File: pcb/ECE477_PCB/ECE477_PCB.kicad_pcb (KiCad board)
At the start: 2 copper layers, 36.5 x 25.4 mm, 64 parts, among them J1 PWR, J2 USB_B_Micro, J3 Micro_SD_Card_Det, J4 DEBUG, J5 DSMX, M1 Brushed_DC, M2 Brushed_DC, M3 Brushed_DC, M4 Brushed_DC, Q1 IRLML6244TR, Q2 IRLML6244TR, Q3 IRLML6244TR, Q4 IRLML6244TR, SW1 SW_Push, U1 AMS1117-3.3, U3 FT230XQ, U4 STM32F446RETx, U5 MPU-6050, Y1 16MHz X322516MLB4SI

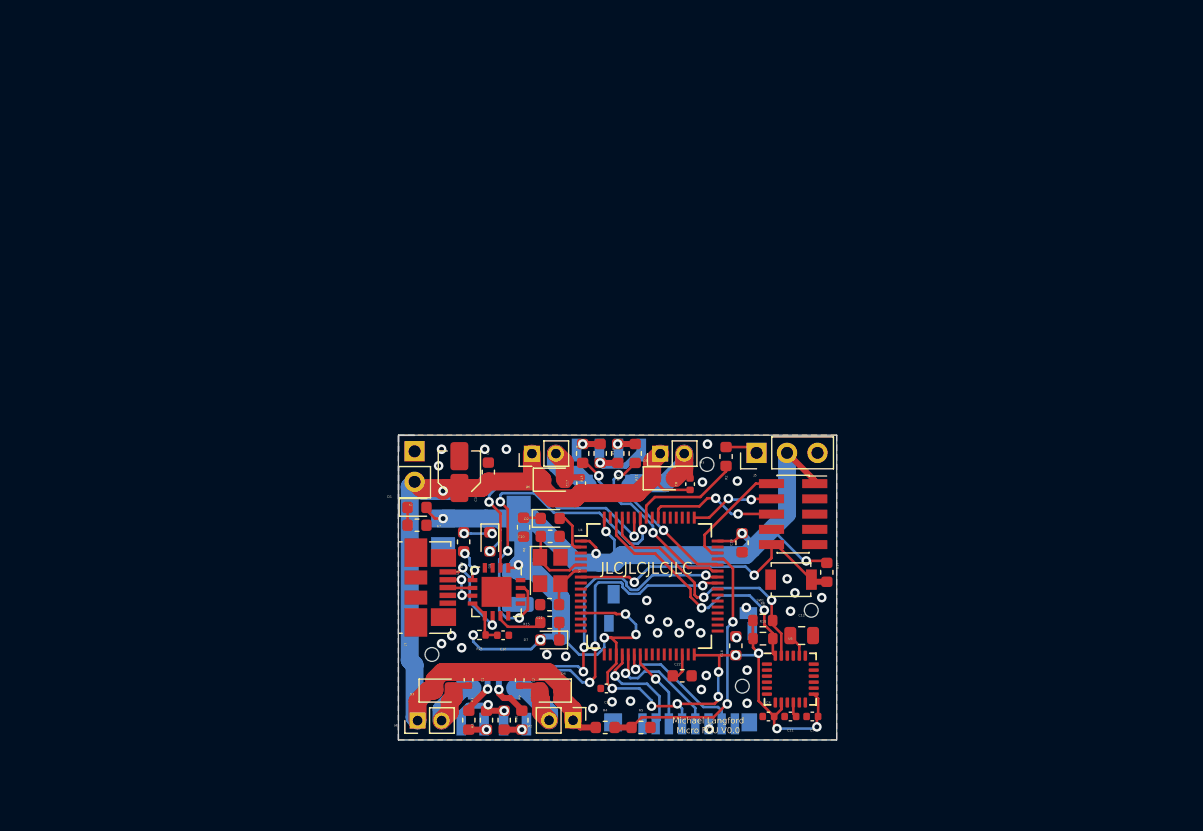
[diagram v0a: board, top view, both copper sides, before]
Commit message: updated PCB to Kicad 6
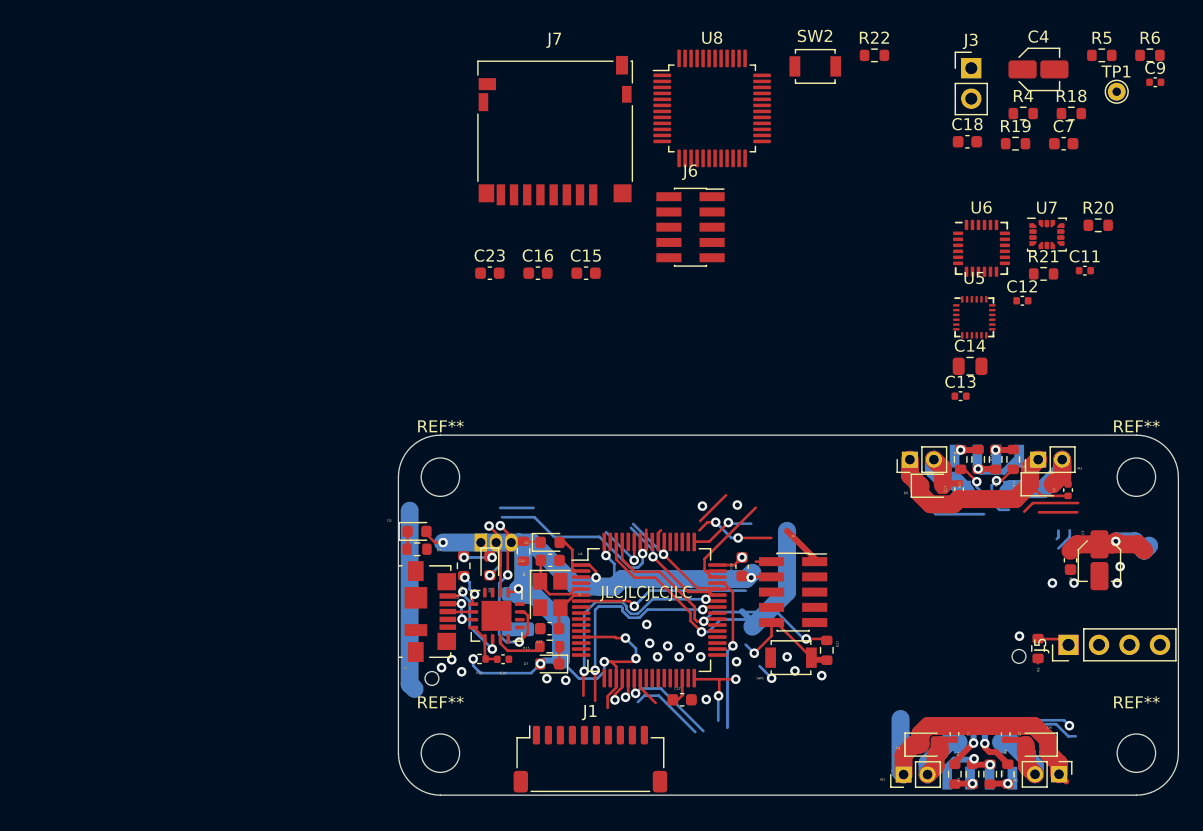
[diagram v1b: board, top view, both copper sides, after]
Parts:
- added C13: 0.1uF 2V, Capacitor_SMD:C_0402_1005Metric, F.Cu at (94.8, 24.7)
- added C14: 2.2nF, 50V, Capacitor_SMD:C_0805_2012Metric, F.Cu at (95.5, 22.2)
- added C15: 2.2uF, Capacitor_SMD:C_0603_1608Metric, F.Cu at (63.5, 14.5)
- added C16: 1uF, Capacitor_SMD:C_0603_1608Metric, F.Cu at (59.5, 14.5)
- added C23: 10nF, Capacitor_SMD:C_0603_1608Metric, F.Cu at (55.5, 14.5)
- added J6: DEBUG, Connector_PinSocket_1.27mm:PinSocket_2x05_P1.27mm_Vertical_SMD, F.Cu at (72.2, 10.6)
- added J7: Micro_SD_Card_Det, Connector_Card:microSD_HC_Hirose_DM3D-SF, F.Cu at (61.0, 2.59)
- added R19: 220, Resistor_SMD:R_0603_1608Metric, F.Cu at (99.3, 3.68)
- added R20: 4.7K, Resistor_SMD:R_0603_1608Metric, F.Cu at (106.2, 10.5)
- added R21: 4.7K, Resistor_SMD:R_0603_1608Metric, F.Cu at (101.7, 14.5)
- added R22: 1K, Resistor_SMD:R_0603_1608Metric, F.Cu at (87.6, -3.68)
- added REF**: MountingHole_3.2mm_M3, MountingHole:MountingHole_3.2mm_M3, F.Cu at (109.4, 31.5)
- added REF**: MountingHole_3.2mm_M3, MountingHole:MountingHole_3.2mm_M3, F.Cu at (109.4, 54.5)
- added REF**: MountingHole_3.2mm_M3, MountingHole:MountingHole_3.2mm_M3, F.Cu at (51.4, 54.5)
- added REF**: MountingHole_3.2mm_M3, MountingHole:MountingHole_3.2mm_M3, F.Cu at (51.4, 31.5)
- added SW2: RESET, Button_Switch_SMD:SW_SPST_B3U-1000P, F.Cu at (82.6, -2.76)
- added TP1: TX, TestPoint:TestPoint_THTPad_D1.5mm_Drill0.7mm, F.Cu at (107.8, -0.65)
- added U6: MPU-6050, Sensor_Motion:InvenSense_QFN-24_4x4mm_P0.5mm, F.Cu at (96.5, 12.4)
- added U7: LSM6DS3, Package_LGA:LGA-14_3x2.5mm_P0.5mm_LayoutBorder3x4y, F.Cu at (101.9, 11.2)
- added U8: STM32F103CBTx, Package_QFP:LQFP-48_7x7mm_P0.5mm, F.Cu at (74.0, 0.74)
- C11: value 0.1uF 2V -> 10nF, 4V
- C12: value 2.2nF, 50V -> 0.1uF 4V; footprint Capacitor_SMD:C_0805_2012Metric -> Capacitor_SMD:C_0402_1005Metric
- C4: value 10nF, 4V -> 100uF; footprint Capacitor_SMD:C_0402_1005Metric -> Capacitor_SMD:C_Elec_3x5.4
- C7: value 0.1uF 4V -> 1uF; footprint Capacitor_SMD:C_0402_1005Metric -> Capacitor_SMD:C_0603_1608Metric
- J1: value PWR -> ESC; footprint Connector_PinHeader_2.54mm:PinHeader_1x02_P2.54mm_Vertical -> Connector_JST:JST_SH_SM10B-SRSS-TB_1x10-1MP_P1.00mm_Horizontal
- J3: value Micro_SD_Card_Det -> AUX_PWR; footprint Connector_Card:microSD_HC_Hirose_DM3D-SF -> Connector_PinHeader_2.54mm:PinHeader_1x02_P2.54mm_Vertical; moved to F.Cu
- J5: value DSMX -> ELRS; footprint Connector_PinHeader_2.54mm:PinHeader_1x03_P2.54mm_Vertical -> Connector_PinHeader_2.54mm:PinHeader_1x04_P2.54mm_Vertical
- R18: value 4.7K -> 220
- R6: value 4.7K -> 0 DNP
- SW1: value SW_Push -> RESET
- U1: value AMS1117-3.3 -> LM78L05_TO92; footprint Package_TO_SOT_SMD:SOT-223-3_TabPin2 -> Package_TO_SOT_THT:TO-92_Inline
- U5: value MPU-6050 -> MPU-9250; footprint Sensor_Motion:InvenSense_QFN-24_4x4mm_P0.5mm -> Sensor_Motion:InvenSense_QFN-24_3x3mm_P0.4mm
- moved C9 68.1 mm to (111.0, -1.44), turned to 0 degrees
- moved R5 67.9 mm to (106.5, -3.68)
- moved R4 61.9 mm to (100.0, 1.17)
- moved C4 58.4 mm to (101.2, -2.51)
- moved R6 57.1 mm to (110.5, -3.68)
- moved J3 54.9 mm to (95.6, -2.61), turned to 0 degrees
- moved C3 53.8 mm to (106.3, 38.4), turned to -90 degrees
- moved C7 52.1 mm to (103.3, 3.68), turned to 0 degrees
- moved R18 50.7 mm to (104.0, 1.17)
- moved C6 49.1 mm to (103.9, 38.4), turned to -90 degrees
- moved C18 46.2 mm to (95.3, 3.52), turned to 0 degrees
- moved C11 44.5 mm to (105.1, 14.3), turned to 0 degrees
- moved M2 40.7 mm to (103.0, 56.2)
- moved R3 40.7 mm to (95.7, 56.2)
- moved C2 40.7 mm to (98.5, 52.9)
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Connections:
- C11 pad 1: Net-(C11-Pad1) -> GND
- C11 pad 2: GND -> +3V3
- C12 pad 1: Net-(C12-Pad1) -> +3V3
- C3 pad 1: +BATT -> +10V
- C4 pad 1: GND -> +5V
- C4 pad 2: +3V3 -> GND
- C6 pad 1: +BATT -> +10V
- C7 pad 1: +3V3 -> +5V
- J1 pad 2: +BATT -> GND
- J2 pad 4: (no net) -> unconnected-(J2-Pad4)
- J3 pad 1: (no net) -> GND
- J3 pad 2: SD_CARD_CS -> +BATT
- J4 pad 7: (no net) -> unconnected-(J4-Pad7)
- J4 pad 8: (no net) -> unconnected-(J4-Pad8)
- J5 pad 2: +3V3 -> Net-(J5-Pad2)
- J5 pad 3: GND -> +5V
- R18 pad 1: +3V3 -> Net-(R4-Pad2)
- R18 pad 2: I2C1_SDA -> unconnected-(R18-Pad2)
- R2 pad 2: DSMX -> ELRS_RX
- R4 pad 2: VSENSE -> Net-(R4-Pad2)
- R5 pad 1: VSENSE -> Net-(R4-Pad2)
- R6 pad 1: +3V3 -> +BATT
- R6 pad 2: I2C1_SCL -> +10V
- U1 pad 1: GND -> +5V
- U1 pad 2: +3V3 -> GND
- U1 pad 3: +BATT -> +10V
- U3 pad 12: (no net) -> unconnected-(U3-Pad12)
- U3 pad 14: (no net) -> unconnected-(U3-Pad14)
- U3 pad 15: USART1_TX -> USART1_RX
- U3 pad 16: (no net) -> unconnected-(U3-Pad16)
- U3 pad 2: USART1_RX -> USART1_TX
- U3 pad 4: (no net) -> unconnected-(U3-Pad4)
- U4 pad 10: (no net) -> unconnected-(U4-Pad10)
- U4 pad 11: (no net) -> unconnected-(U4-Pad11)
- U4 pad 14: (no net) -> unconnected-(U4-Pad14)
- U4 pad 15: (no net) -> unconnected-(U4-Pad15)
- U4 pad 16: (no net) -> unconnected-(U4-Pad16)
- U4 pad 17: (no net) -> unconnected-(U4-Pad17)
- U4 pad 24: (no net) -> unconnected-(U4-Pad24)
- U4 pad 25: (no net) -> unconnected-(U4-Pad25)
- U4 pad 26: (no net) -> unconnected-(U4-Pad26)
- U4 pad 27: (no net) -> unconnected-(U4-Pad27)
- U4 pad 28: (no net) -> unconnected-(U4-Pad28)
- U4 pad 29: (no net) -> unconnected-(U4-Pad29)
- U4 pad 3: (no net) -> unconnected-(U4-Pad3)
- U4 pad 33: (no net) -> unconnected-(U4-Pad33)
- U4 pad 34: (no net) -> unconnected-(U4-Pad34)
- U4 pad 35: (no net) -> unconnected-(U4-Pad35)
- U4 pad 36: (no net) -> unconnected-(U4-Pad36)
- U4 pad 37: (no net) -> unconnected-(U4-Pad37)
- U4 pad 38: (no net) -> unconnected-(U4-Pad38)
- U4 pad 39: (no net) -> unconnected-(U4-Pad39)
- U4 pad 4: (no net) -> unconnected-(U4-Pad4)
- U4 pad 40: (no net) -> unconnected-(U4-Pad40)
- U4 pad 50: (no net) -> unconnected-(U4-Pad50)
- U4 pad 51: (no net) -> unconnected-(U4-Pad51)
- U4 pad 52: (no net) -> unconnected-(U4-Pad52)
- U4 pad 53: (no net) -> unconnected-(U4-Pad53)
- U4 pad 54: (no net) -> unconnected-(U4-Pad54)
- U4 pad 56: (no net) -> unconnected-(U4-Pad56)
- U4 pad 8: (no net) -> unconnected-(U4-Pad8)
- U4 pad 9: (no net) -> unconnected-(U4-Pad9)
- U5 pad 1: (no net) -> unconnected-(U5-Pad1)
- U5 pad 10: Net-(C11-Pad1) -> unconnected-(U5-Pad10)
- U5 pad 11: (no net) -> unconnected-(U5-Pad11)
- U5 pad 12: (no net) -> unconnected-(U5-Pad12)
- U5 pad 13: +3V3 -> unconnected-(U5-Pad13)
- U5 pad 18: GND -> unconnected-(U5-Pad18)
- U5 pad 20: Net-(C12-Pad1) -> unconnected-(U5-Pad20)
- U5 pad 21: (no net) -> unconnected-(U5-Pad21)
- U5 pad 22: (no net) -> unconnected-(U5-Pad22)
- U5 pad 23: I2C1_SCL -> unconnected-(U5-Pad23)
- U5 pad 24: I2C1_SDA -> unconnected-(U5-Pad24)
- U5 pad 7: (no net) -> unconnected-(U5-Pad7)
- U5 pad 8: +3V3 -> unconnected-(U5-Pad8)
- U5 pad 9: GND -> unconnected-(U5-Pad9)
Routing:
- net USART1_TX: track 31.3 -> 0.77 mm, vias 4 -> 0
- net VSENSE: track 23.3 -> 51.8 mm, vias 2 -> 5
- net +3V3: track 143.2 -> 171.2 mm, vias 21 -> 23
- net I2C1_SDA: track 21.8 -> 0.00 mm, vias 2 -> 0
- net I2C1_SCL: track 22.3 -> 1.44 mm, vias 2 -> 1
- net MOTOR_A: track 31.5 -> 12.0 mm, vias 4 -> 2
- net +BATT: track 77.0 -> 60.0 mm, vias 1 -> 0
- net DSMX: track 9.28 -> 24.3 mm, vias 0 -> 1
- net +10V: track 0.00 -> 11.3 mm, vias 0 -> 1
- net MOTOR_D: track 15.6 -> 5.70 mm, vias 2 -> 1
- net MOTOR_C: track 14.5 -> 5.23 mm, vias 2 -> 1
- net SD_CARD_CS: track 8.93 -> 2.04 mm
- net USART1_RX: track 22.3 -> 16.4 mm, vias 2 -> 1
- net SPI1_MOSI: track 6.77 -> 2.58 mm, vias 1 -> 0
- net Net-(C20-Pad1): track 5.96 -> 9.89 mm
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- removed copper zone on B.Cu, net GND
- removed copper zone on F.Cu, net GND
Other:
- board size 36.5 x 25.4 mm -> 65 x 30 mm
- net class Default removed
- net class Power removed
- net class Power2 removed
- net class Power3 removed
- board text removed: "Michael Langford Micro FCU V0.0"

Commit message: modified layout of motor control and power, added minimal initial schematic for LiDAR and footprints
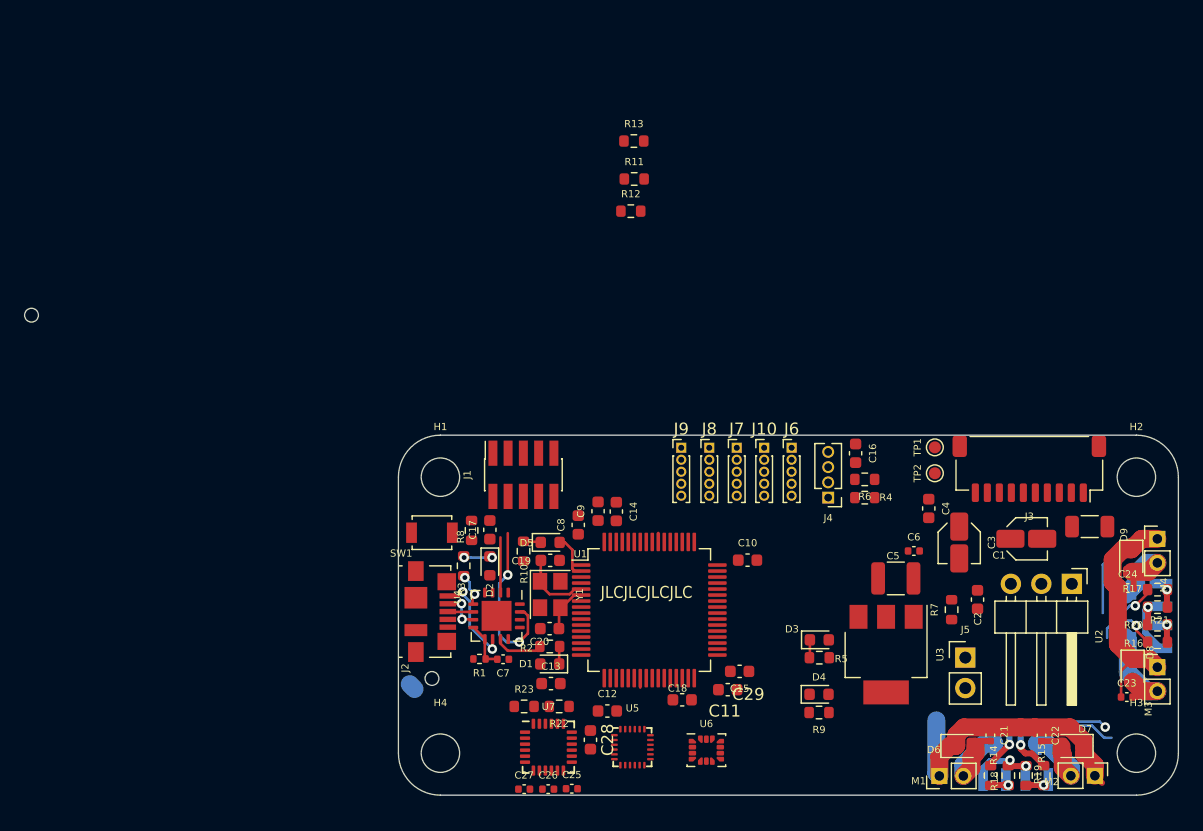
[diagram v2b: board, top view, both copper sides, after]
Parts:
- removed the C15 at (63.5, 14.5)
- removed the C19 at (76.5, 38.9)
- removed the C23 at (55.5, 14.5)
- removed the R22 at (87.6, -3.68)
- removed SW2: RESET, Button_Switch_SMD:SW_SPST_B3U-1000P
- removed U8: STM32F103CBTx, Package_QFP:LQFP-48_7x7mm_P0.5mm
- added C10: 0.1uF, Capacitor_SMD:C_0603_1608Metric, F.Cu at (77.0, 38.4)
- added C11: 10nF, Capacitor_SMD:C_0603_1608Metric, F.Cu at (75.3, 49.2)
- added C12: 0.1uF, Capacitor_SMD:C_0603_1608Metric, F.Cu at (65.3, 51.0)
- added C13: 0.1uF, Capacitor_SMD:C_0603_1608Metric, F.Cu at (60.6, 48.7)
- added C14: 0.1uF, Capacitor_SMD:C_0603_1608Metric, F.Cu at (66.1, 34.3)
- added C17: 1uF, Capacitor_SMD:C_0603_1608Metric, F.Cu at (55.5, 35.9)
- added C29: 33uF 35V, Capacitor_SMD:C_1206_3216Metric, F.Cu at (105.5, 35.6)
- added C8: 0.1uF, Capacitor_SMD:C_0603_1608Metric, F.Cu at (62.9, 35.4)
- added C9: 0.1uF, Capacitor_SMD:C_0603_1608Metric, F.Cu at (64.5, 34.3)
- added D4: 5V, LED_SMD:LED_0603_1608Metric, F.Cu at (83.0, 49.6)
- added J10: ToF 5, Connector_PinHeader_1.00mm:PinHeader_1x05_P1.00mm_Vertical, F.Cu at (78.4, 29.0)
- added J8: ToF 3, Connector_PinHeader_1.00mm:PinHeader_1x05_P1.00mm_Vertical, F.Cu at (73.8, 29.0)
- added J9: ToF 4, Connector_PinHeader_1.00mm:PinHeader_1x05_P1.00mm_Vertical, F.Cu at (71.5, 29.0)
- added R9: 4.7k, Resistor_SMD:R_0603_1608Metric, F.Cu at (83.0, 51.1)
- added TP2: CRT, TestPoint:TestPoint_Pad_D1.0mm, F.Cu at (92.6, 31.1)
- added U3: REG1117-3.3, Package_TO_SOT_SMD:SOT-223, F.Cu at (88.5, 46.3)
- C28: renamed from C14; footprint Capacitor_SMD:C_0805_2012Metric -> Capacitor_SMD:C_0603_1608Metric
- C5: moved to F.Cu
- D3: renamed from D1; value LED -> 3.3V
- D5: renamed from D2; value LED -> ST
- H1, H2, H3, H4: renamed from REF**; value MountingHole_3.2mm_M3 -> MountingHole
- J4: renamed from J5; footprint Connector_PinHeader_2.54mm:PinHeader_1x04_P2.54mm_Vertical -> Connector_PinHeader_1.27mm:PinHeader_1x04_P1.27mm_Vertical
- J6: value DEBUG -> ToF 1; footprint Connector_PinSocket_1.27mm:PinSocket_2x05_P1.27mm_Vertical_SMD -> Connector_PinHeader_1.00mm:PinHeader_1x05_P1.00mm_Vertical
- J7: value Micro_SD_Card_Det -> ToF 2; footprint Connector_Card:microSD_HC_Hirose_DM3D-SF -> Connector_PinHeader_1.00mm:PinHeader_1x05_P1.00mm_Vertical
- TP1: footprint TestPoint:TestPoint_THTPad_D1.5mm_Drill0.7mm -> TestPoint:TestPoint_Pad_D1.0mm
- U2: renamed from U1; value LM78L05_TO92 -> Pololu_S13V10F5; footprint Package_TO_SOT_THT:TO-92_Inline -> Connector_PinHeader_2.54mm:PinHeader_1x03_P2.54mm_Horizontal; moved to F.Cu
- moved C25 60.8 mm to (62.4, 57.4)
- moved R22 60.2 mm to (61.3, 50.6), turned to 180 degrees
- moved C26 56.7 mm to (60.4, 57.5)
- moved R23 56.3 mm to (58.4, 50.6)
- moved U7 55.1 mm to (60.4, 54.0)
- moved U6 51.5 mm to (73.6, 54.2)
- moved U2 49.4 mm to (104.0, 40.4), turned to -90 degrees
- moved J5 49.1 mm to (95.1, 46.5)
- moved R7 49.1 mm to (94.0, 42.5), turned to 90 degrees
- moved C27 48.9 mm to (58.4, 57.5)
- moved C15 48.0 mm to (76.3, 47.7), turned to 180 degrees
- moved U5 45.8 mm to (67.4, 54.0)
- moved C28 44.4 mm to (63.9, 53.4), turned to -90 degrees
- moved C6 43.9 mm to (90.9, 37.6)
- moved J3 43.9 mm to (100.5, 30.8), turned to 180 degrees
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- renumbered C3 to C1, C18 to C15, C22 to C18, C20 to C19, C6 to C2, C21 to C20, C1 to C21, C2 to C22, C8 to C23, C17 to C24, C11 to C25, C12 to C26, C13 to C27, C4 to C3, C7 to C4, C9 to C6, C10 to C7, D7 to D1, D8 to D2, D3 to D6, D4 to D7, D5 to D8, D6 to D9, J4 to J1, J1 to J3, J3 to J5, R25 to R1, R8 to R10, R4 to R11, R18 to R12, R5 to R13, R1 to R14, R9 to R15, R11 to R16, R13 to R17, R3 to R18, R10 to R19, R15 to R2, R12 to R20, R14 to R21, R20 to R22, R21 to R23, R16 to R3, R2 to R4, R7 to R5, R19 to R6, R6 to R7, R17 to R8, U4 to U1, U3 to U4, U7 to U6, U6 to U7
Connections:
- C15 pad 1: +3V3 -> GND
- C15 pad 2: GND -> +3V3
- C16 pad 1: +3V3 -> GND
- C16 pad 2: GND -> +5V
- J6 pad 1: +3V3 -> GND
- J6 pad 2: SYS_JTMS-SWDIO -> +3.3V
- J6 pad 3: GND -> TOF_SCLK
- J6 pad 4: SYS_JTCL-SWCLK -> TOF_SDA
- J6 pad 5: GND -> TOF_1_SHTDN
- J7 pad 1: unconnected-(J7-Pad1) -> GND
- J7 pad 2: SD_CARD_CS -> +3.3V
- J7 pad 3: SPI1_MOSI -> TOF_SCLK
- J7 pad 4: +3V3 -> TOF_SDA
- J7 pad 5: SPI1_SCK -> TOF_2_SHTDN
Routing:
- net +3V3: track 171.2 -> 0.00 mm, vias 23 -> 0
- net VSENSE: track 51.8 -> 0.00 mm, vias 5 -> 0
- net DSMX: track 24.3 -> 0.00 mm, vias 1 -> 0
- net NRST: track 24.1 -> 0.00 mm, vias 2 -> 0
- net MOTOR_B: track 31.0 -> 12.2 mm, vias 3 -> 1
- net +BATT: track 60.0 -> 45.6 mm
- net +10V: track 11.3 -> 0.00 mm, vias 1 -> 0
- net SYS_JTCL-SWO: track 11.1 -> 0.72 mm, vias 2 -> 0
- net Net-(C20-Pad1): track 0.00 -> 9.89 mm
- net Net-(C19-Pad1): track 9.89 -> 0.00 mm
- net SYS_JTMS-SWDIO: track 9.61 -> 0.00 mm
- net SPI1_MISO: track 8.57 -> 0.00 mm, vias 1 -> 0
- net SPI1_SCK: track 7.92 -> 0.00 mm, vias 1 -> 0
- net SYS_JTCL-SWCLK: track 5.44 -> 0.00 mm, vias 1 -> 0
- net USART1_RX: track 16.4 -> 21.0 mm, vias 1 -> 2
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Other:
- board size 65 x 30 mm -> 96.2 x 40.6 mm

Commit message: updated schematic I2C and UART connections
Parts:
- removed U7: MPU-6050, Sensor_Motion:InvenSense_QFN-24_4x4mm_P0.5mm
- added R24: 4.7K, Resistor_SMD:R_0603_1608Metric, F.Cu at (83.3, 31.3)
- added R25: 4.7K, Resistor_SMD:R_0603_1608Metric, F.Cu at (83.3, 32.8)
- C10, C11, C12, C13, C14, C15, C16, C18, C25, C26, C27, C28, C29, C4, C5, C6, C8, C9, R22, R23, U3: moved to B.Cu
- H1, H2, H3, H4: value MountingHole -> M3
- J2: footprint Connector_USB:USB_Micro-B_Molex_47346-0001 -> Connector_USB:USB_Micro-B_Molex-105017-0001
- J4: footprint Connector_PinHeader_1.27mm:PinHeader_1x04_P1.27mm_Vertical -> Connector_PinSocket_1.27mm:PinSocket_1x04_P1.27mm_Vertical
- moved R13 46.0 mm to (75.4, 48.8), turned to 90 degrees
- moved R11 43.2 mm to (76.9, 48.8), turned to 90 degrees
- moved R12 41.1 mm to (78.4, 48.8), turned to -90 degrees
- moved J4 34.6 mm to (57.5, 55.8)
- moved C16 34.4 mm to (60.4, 52.5)
- moved R4 34.4 mm to (61.2, 56.2)
- moved R6 34.4 mm to (61.2, 54.6)
- moved R23 17.7 mm to (75.8, 53.4), turned to 180 degrees
- moved C25 17.3 mm to (79.6, 56.7), turned to 180 degrees
- moved C26 17.3 mm to (77.7, 56.7), turned to 180 degrees
- moved C27 17.3 mm to (75.7, 56.7), turned to 180 degrees
- moved R22 15.3 mm to (76.0, 55.0), turned to 0 degrees
- moved C28 14.5 mm to (78.4, 54.3)
- moved D3 7.95 mm to (90.7, 43.2)
- moved D4 7.95 mm to (90.7, 47.8)
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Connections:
- C27 pad 1: Net-(C27-Pad1) -> unconnected-(C27-Pad1)
- C28 pad 1: Net-(C28-Pad1) -> unconnected-(C28-Pad1)
- J1 pad 1: +3V3 -> SYS_JTMS-SWDIO
- J1 pad 10: NRST -> GND
- J1 pad 2: SYS_JTMS-SWDIO -> +3V3
- J1 pad 3: GND -> SYS_JTCL-SWCLK
- J1 pad 4: SYS_JTCL-SWCLK -> GND
- J1 pad 5: GND -> SYS_JTCL-SWO
- J1 pad 6: SYS_JTCL-SWO -> GND
- J1 pad 9: GND -> NRST
- J10 pad 3: TOF_SCLK -> I2C1_SCL
- J10 pad 4: TOF_SDA -> I2C1_SDA
- J6 pad 3: TOF_SCLK -> I2C1_SCL
- J6 pad 4: TOF_SDA -> I2C1_SDA
- J7 pad 3: TOF_SCLK -> I2C1_SCL
- J7 pad 4: TOF_SDA -> I2C1_SDA
- J8 pad 3: TOF_SCLK -> I2C1_SCL
- J8 pad 4: TOF_SDA -> I2C1_SDA
- J9 pad 3: TOF_SCLK -> I2C1_SCL
- J9 pad 4: TOF_SDA -> I2C1_SDA
- R22 pad 2: I2C1_SCL -> unconnected-(R22-Pad2)
- R23 pad 2: I2C1_SDA -> unconnected-(R23-Pad2)
- U1 pad 16: unconnected-(U1-Pad16) -> ELRS_RX
- U1 pad 17: unconnected-(U1-Pad17) -> ELRS_TX
- U1 pad 20: SD_CARD_CS -> unconnected-(U1-Pad20)
- U1 pad 45: VSENSE -> unconnected-(U1-Pad45)
- U1 pad 51: unconnected-(U1-Pad51) -> UART4_RX
- U1 pad 52: unconnected-(U1-Pad52) -> UART4_TX
- U1 pad 57: DSMX -> unconnected-(U1-Pad57)
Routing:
- net I2C1_SCL: track 0.00 -> 26.9 mm, vias 0 -> 1
- net I2C1_SDA: track 0.00 -> 25.9 mm, vias 0 -> 1
- net NRST: track 0.00 -> 22.9 mm, vias 0 -> 2
- net USART1_TX: track 4.54 -> 18.1 mm
- net SYS_JTMS-SWDIO: track 0.00 -> 12.1 mm
- net SYS_JTCL-SWCLK: track 0.00 -> 9.07 mm
- net SYS_JTCL-SWO: track 0.72 -> 8.33 mm
- net Net-(C19-Pad1): track 0.00 -> 6.45 mm
- net Net-(C20-Pad1): track 9.89 -> 4.64 mm
- net USART1_RX: track 21.0 -> 26.3 mm
- net +3V3: track 0.00 -> 3.77 mm
- net +BATT: track 45.6 -> 45.0 mm
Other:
- outline, holes or cut-outs redrawn
